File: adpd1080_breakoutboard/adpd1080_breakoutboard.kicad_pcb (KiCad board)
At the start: 2 copper layers, 43 x 39 mm, 27 parts, among them IC1 ADPD1080BCPZR7, J1 1V8_IN, J2 3V3_IN, J3 PG_TP, J4 P_05, J5 P_01, J6 PD_7, J7 P_3_LED, J8 P_1, U1 LD39100 1V8, U2 TXB0104PW_new

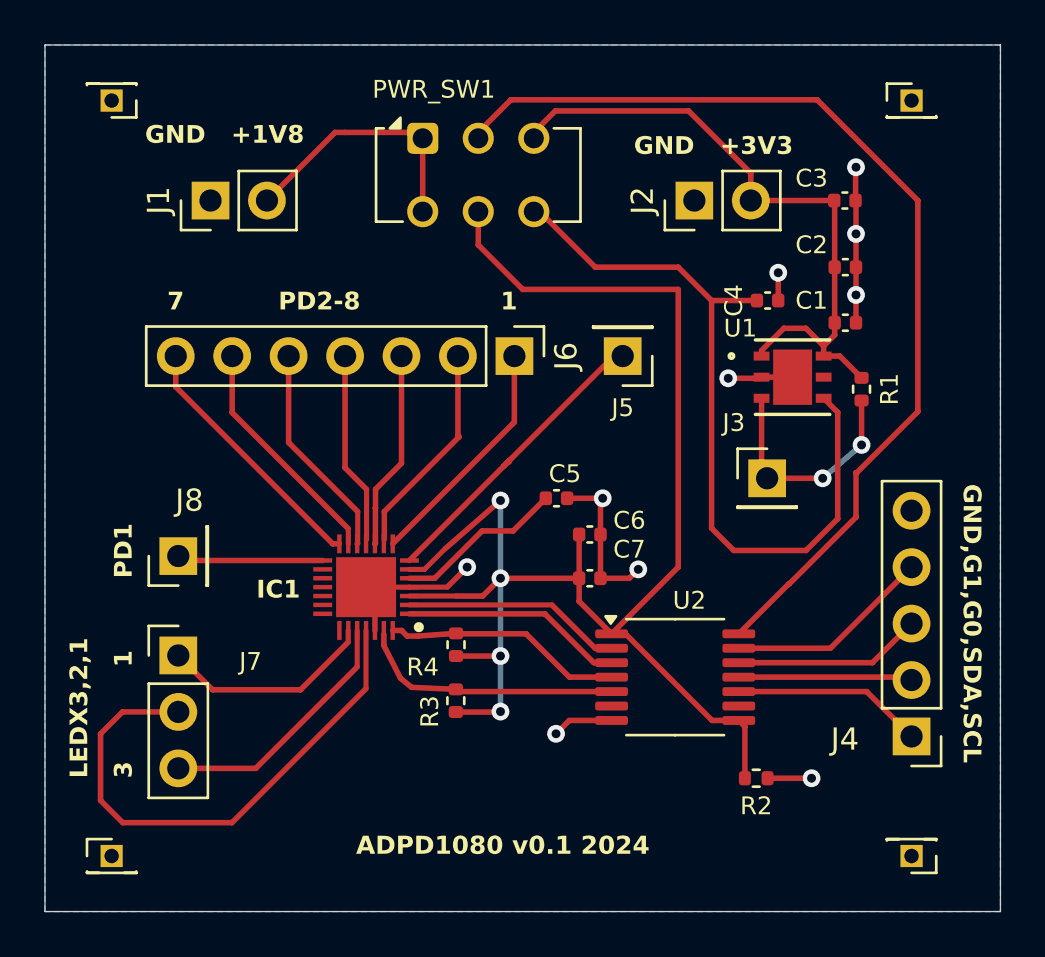
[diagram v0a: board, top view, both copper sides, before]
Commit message: replace txb0104 with txs0104e for i2c
- txb0104 does not work with i2c but txs0104e works
- changed the i2c pull-ups to 'no-placement' because
  the txs0104e has internal 10k pull-ups
- added test points for 1v8 logic scl and sda

Signed-off-by: Mika Laitio <lamikr@gmail.com>
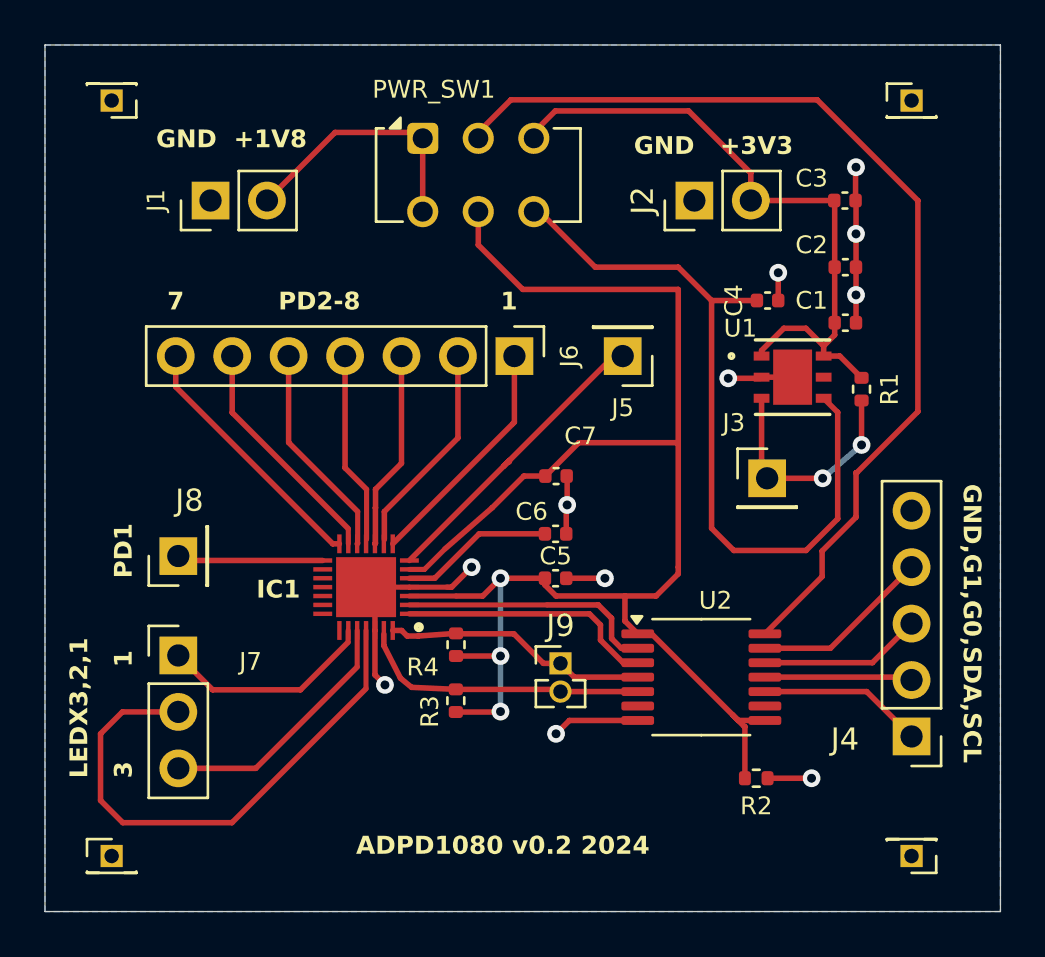
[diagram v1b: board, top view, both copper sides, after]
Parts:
- added J9: I2C_TP, Connector_PinHeader_1.27mm:PinHeader_1x02_P1.27mm_Vertical, F.Cu at (43.2, 47.8)
- C5: value 1uF -> 0u1F
- C6: value 0u1F -> 1uF
- U2: value TXB0104PW_new -> TXS0104E
- moved C7 4.84 mm to (43.0, 39.4)
- moved C5 3.60 mm to (43.0, 44.0)
- moved C6 1.54 mm to (43.0, 42.0)
- moved U2 1.18 mm to (49.5, 48.5)
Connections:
- C5 pad 1: Net-(IC1-VREF) -> VDD_1V8
- C6 pad 1: VDD_1V8 -> Net-(IC1-VREF)
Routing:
- net VDD_1V8: track 70.3 -> 74.5 mm, vias 4 -> 3
- net Net-(IC1-GPIO1): track 9.91 -> 11.6 mm
- net Net-(IC1-GPIO0): track 10.0 -> 11.6 mm
- net Net-(IC1-SDA): track 10.8 -> 11.9 mm
- net Net-(J4-Pin_4): track 9.29 -> 8.11 mm
- net Net-(J4-Pin_2): track 7.83 -> 6.65 mm
- net Net-(J4-Pin_1): track 8.61 -> 7.44 mm
- net Net-(IC1-SCL): track 11.9 -> 13.0 mm
- net Net-(J4-Pin_3): track 8.50 -> 7.33 mm
- net GND: track 29.6 -> 30.6 mm, vias 10 -> 11
- net Net-(J3-Pin_1): track 11.0 -> 10.2 mm
- net Net-(IC1-VREF): track 7.63 -> 6.97 mm
- net VDD_INPUT: track 45.1 -> 44.6 mm
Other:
- board text added: "ADPD1080 v0.2 2024"
- board text removed: "ADPD1080 v0.1 2024"
